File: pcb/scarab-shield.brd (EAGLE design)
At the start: 51.7 x 76.2 mm, 10 parts

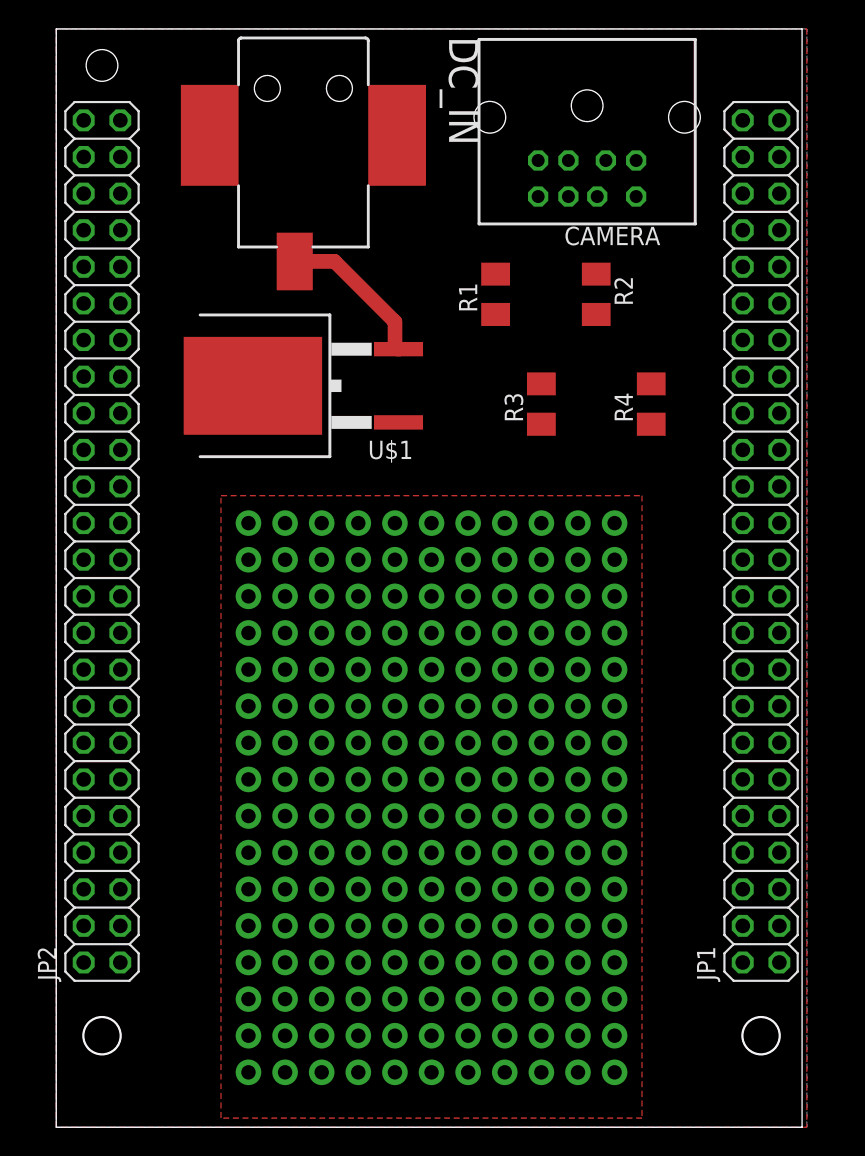
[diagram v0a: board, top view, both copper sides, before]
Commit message: finished new camera shield
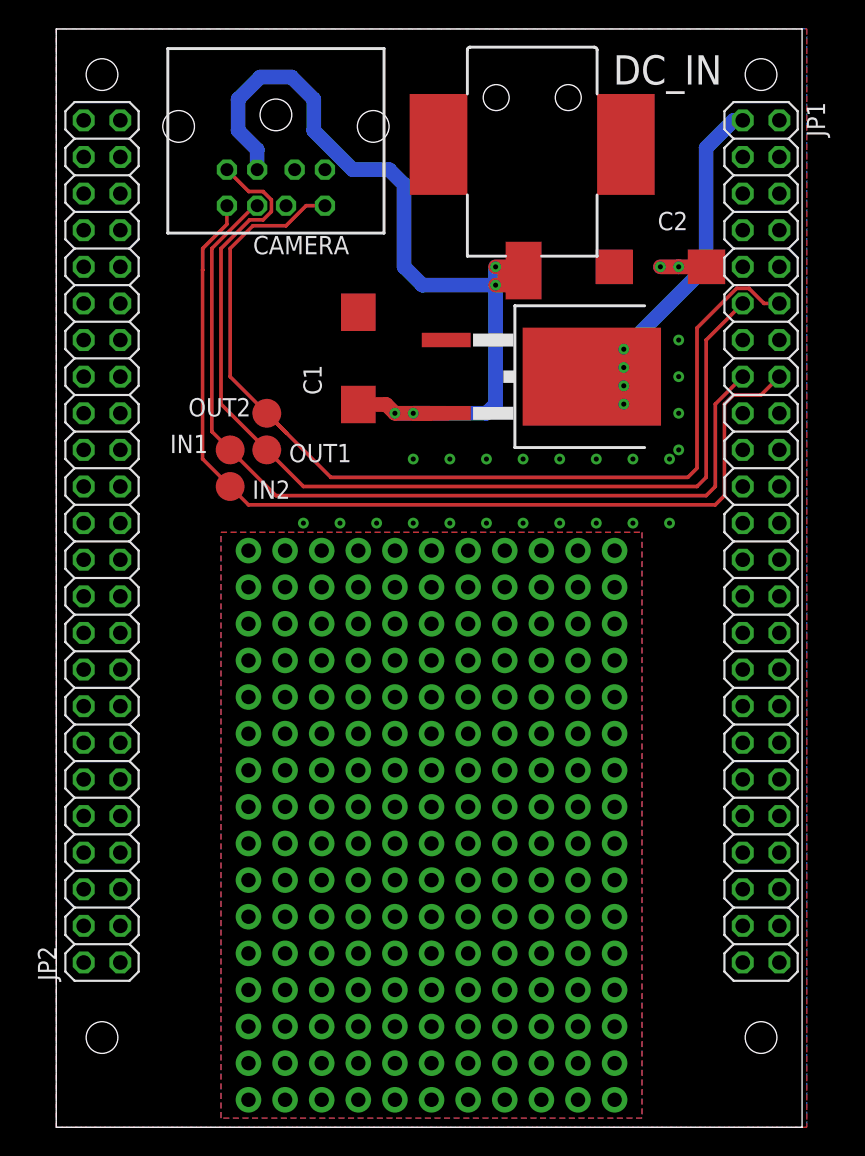
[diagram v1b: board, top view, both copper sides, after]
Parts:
- removed R1, R2, R3, R4: (no value), rcl:M1206
- added C1, C2: (no value), rcl:CT7343
- added IN1, IN2, OUT1, OUT2: TPTP20R, testpad:TP20R
- moved CAMERA 21.6 mm to (15.2, 74.9)
- moved U$1 16.5 mm to (33.7, 52.1), turned to 270 degrees
- moved DC_IN 15.9 mm to (33.0, 74.9)
- moved JP1 2.54 mm to (48.9, 41.9), turned to 270 degrees
- moved U$2 1.91 mm to (21.0, 42.5)
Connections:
- net GND: now also C1.-, C2.-, JP1.2
- net SYNC_IN1: now also IN1.TP, JP1.15
- net SYNC_IN2: now also IN2.TP, JP1.16
- net SYNC_OUT1: now also JP1.11, OUT1.TP
- net SYNC_OUT2: now also JP1.12, OUT2.TP
- net VCC: now also C2.+, JP1.1
- net VIN: now also C1.+
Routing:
- net SYNC_OUT2: track 0.00 -> 71.2 mm
- net SYNC_OUT1: track 0.00 -> 69.9 mm
- net SYNC_IN2: track 0.00 -> 67.2 mm
- net SYNC_IN1: track 0.00 -> 62.7 mm
- net VIN: track 10.7 -> 63.8 mm, vias 0 -> 4
- net VCC: track 0.00 -> 33.0 mm, vias 0 -> 6
- added copper zone on layer 16, net N$2
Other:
- outline, holes or cut-outs redrawn
